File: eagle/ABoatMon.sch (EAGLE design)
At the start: 28 parts, among them J1 VUSB, J2 GND, J3 GND, X1 MKDSN1,5/2-5,08

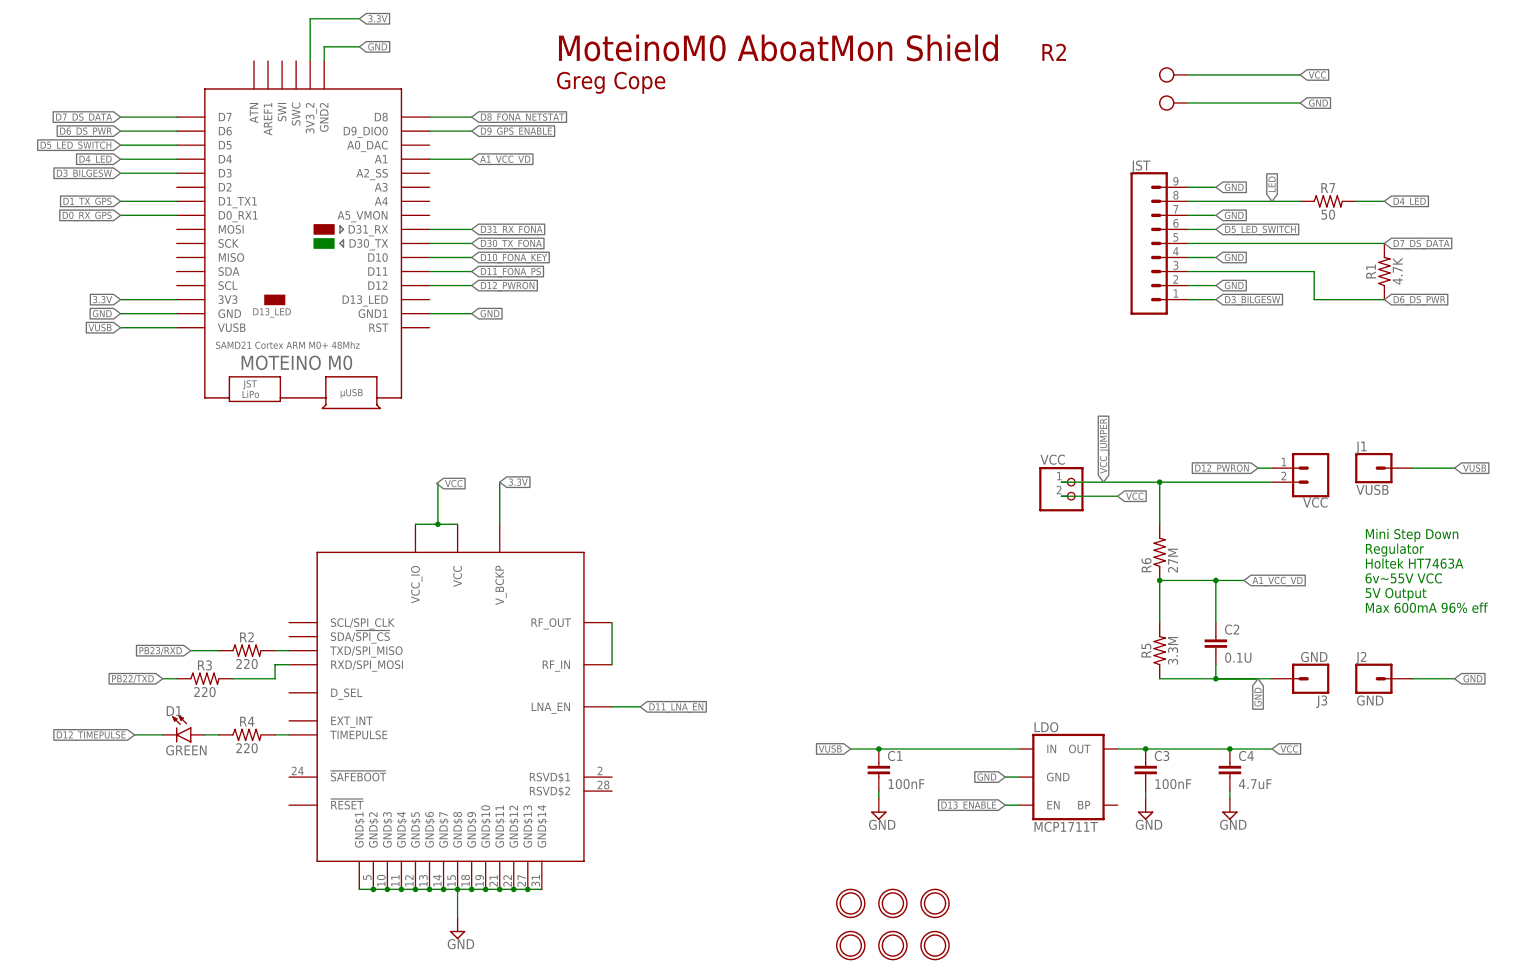
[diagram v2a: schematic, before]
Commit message: started adding nets
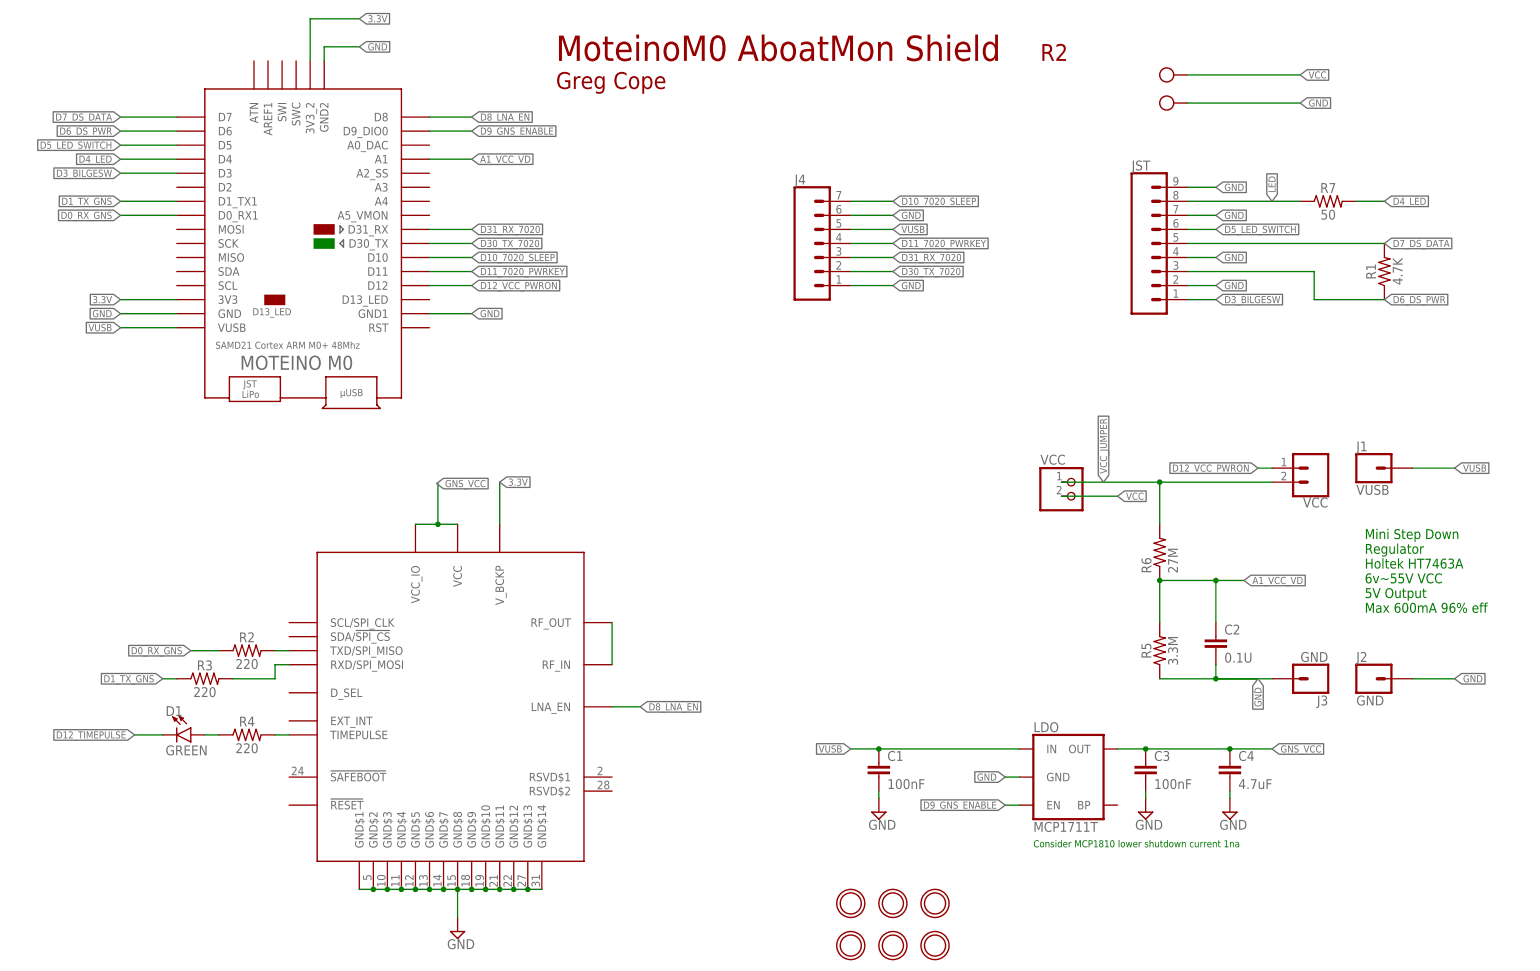
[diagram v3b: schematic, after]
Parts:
- added J4: (no value), SparkFun-Connectors:CONN_07
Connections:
- net D12_PWRON renamed D12_VCC_PWRON
- removed net D0_RX_GPS: U$6.D0_RX1
- removed net D10_FONA_KEY: U$6.D10
- removed net D11_FONA_PS: U$6.D11
- removed net D11_LNA_EN: U$5.LNA_EN
- removed net D13_ENABLE: LDO.EN
- removed net D1_TX_GPS: U$6.D1_TX1
- removed net D30_TX_FONA: U$6.D30_TX
- removed net D31_RX_FONA: U$6.D31_RX
- removed net D8_FONA_NETSTAT: U$6.D8
- removed net D9_GPS_ENABLE: U$6.D9_DIO0
- removed net PB22/TXD: R3.1
- removed net PB23/RXD: R2.1
- new net D0_RX_GNS: R2.1, U$6.D0_RX1
- new net D10_7020_SLEEP: J4.7, U$6.D10
- new net D11_7020_PWRKEY: J4.4, U$6.D11
- new net D1_TX_GNS: R3.1, U$6.D1_TX1
- new net D30_TX_7020: J4.2, U$6.D30_TX
- new net D31_RX_7020: J4.3, U$6.D31_RX
- new net D8_LNA_EN: U$5.LNA_EN, U$6.D8
- new net D9_GNS_ENABLE: LDO.EN, U$6.D9_DIO0
- new net GNS_VCC: C3.1, C4.1, LDO.OUT, U$5.VCC, U$5.VCC_IO
- net GND: now also J4.1, J4.6
- net VCC: no longer C3.1, C4.1, LDO.OUT, U$5.VCC, U$5.VCC_IO
- net VUSB: now also J4.5
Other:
- note added: "Consider MCP1810 lower shutdown current 1na"
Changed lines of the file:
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@@
 <part name="SUPPLY5" library="supply2" library_urn="urn:adsk.eagle:library:372" deviceset="GND" device=""/>
 <part name="D1" library="SparkFun-LED" library_urn="urn:adsk.eagle:library:529" deviceset="LED-GREEN" device="0603" package3d_urn="urn:adsk.eagle:package:39354/1" value="GREEN"/>
+<part name="J4" library="SparkFun-Connectors" library_urn="urn:adsk.eagle:library:513" deviceset="CONN_07" device="" package3d_urn="urn:adsk.eagle:package:38129/1"/>
 </parts>
 <sheets>
@@
 <text x="189.23" y="167.64" size="3.048" layer="94" ratio="12">R2</text>
 <text x="101.6" y="167.64" size="4.572" layer="94" ratio="15">MoteinoM0 AboatMon Shield</text>
+<text x="187.96" y="25.4" size="1.27" layer="91">Consider MCP1810 lower shutdown current 1na</text>
 </plain>
 <instances>
@@
 <attribute name="NAME" x="30.988" y="49.149" size="1.778" layer="95" font="vector"/>
 <attribute name="VALUE" x="30.988" y="43.815" size="1.778" layer="96" font="vector" align="top-left"/>
+</instance>
+<instance part="J4" gate="G$1" x="149.86" y="132.08" smashed="yes">
+<attribute name="VALUE" x="144.78" y="122.174" size="1.778" layer="96" font="vector"/>
+<attribute name="NAME" x="144.78" y="145.288" size="1.778" layer="95" font="vector"/>
 </instance>
 </instances>
@@
 <wire x1="223.52" y1="35.56" x2="223.52" y2="34.29" width="0.1524" layer="91"/>
 </segment>
+<segment>
+<pinref part="J4" gate="G$1" pin="1"/>
+<wire x1="154.94" y1="127" x2="162.56" y2="127" width="0.1524" layer="91"/>
+<label x="162.56" y="127" size="1.27" layer="95" xref="yes"/>
+</segment>
+<segment>
+<pinref part="J4" gate="G$1" pin="6"/>
+<wire x1="154.94" y1="139.7" x2="162.56" y2="139.7" width="0.1524" layer="91"/>
+<label x="162.56" y="139.7" size="1.27" layer="95" xref="yes"/>
+</segment>
 </net>
 <net name="VUSB" class="1">
@@
 <label x="154.94" y="43.18" size="1.27" layer="95" rot="R180" xref="yes"/>
 </segment>
+<segment>
+<pinref part="J4" gate="G$1" pin="5"/>
+<wire x1="154.94" y1="137.16" x2="162.56" y2="137.16" width="0.1524" layer="91"/>
+<label x="162.56" y="137.16" size="1.27" layer="95" xref="yes"/>
+</segment>
 </net>
 <net name="3.3V" class="1">
@@
 </segment>
 </net>
-<net name="D30_TX_FONA" class="0">
+<net name="D30_TX_7020" class="0">
 <segment>
 <wire x1="78.74" y1="134.62" x2="86.36" y2="134.62" width="0.1524" layer="91"/>
@@
 <label x="86.36" y="134.62" size="1.27" layer="95" xref="yes"/>
 </segment>
-</net>
-<net name="D8_FONA_NETSTAT" class="0">
-<segment>
-<pinref part="U$6" gate="G$1" pin="D8"/>
-<wire x1="78.74" y1="157.48" x2="86.36" y2="157.48" width="0.1524" layer="91"/>
-<label x="86.36" y="157.48" size="1.27" layer="95" xref="yes"/>
+<segment>
+<pinref part="J4" gate="G$1" pin="2"/>
+<wire x1="154.94" y1="129.54" x2="162.56" y2="129.54" width="0.1524" layer="91"/>
+<label x="162.56" y="129.54" size="1.27" layer="95" xref="yes"/>
 </segment>
 </net>
@@
 <pinref part="X1" gate="-1" pin="KL"/>
 <label x="236.22" y="165.1" size="1.27" layer="95" xref="yes"/>
-</segment>
-<segment>
-<pinref part="U$5" gate="G$1" pin="VCC_IO"/>
-<pinref part="U$5" gate="G$1" pin="VCC"/>
-<wire x1="76.2" y1="83.82" x2="80.264" y2="83.82" width="0.1524" layer="91"/>
-<label x="80.01" y="91.186" size="1.27" layer="95" xref="yes"/>
-<wire x1="80.264" y1="83.82" x2="83.82" y2="83.82" width="0.1524" layer="91"/>
-<wire x1="80.264" y1="91.186" x2="80.264" y2="83.82" width="0.1524" layer="91"/>
-<junction x="80.264" y="83.82"/>
-</segment>
-<segment>
-<pinref part="C3" gate="G$1" pin="1"/>
-<pinref part="LDO" gate="G$1" pin="OUT"/>
-<wire x1="203.2" y1="43.18" x2="208.28" y2="43.18" width="0.1524" layer="91"/>
-<junction x="208.28" y="43.18"/>
-<wire x1="208.28" y1="43.18" x2="223.52" y2="43.18" width="0.1524" layer="91"/>
-<label x="231.14" y="43.18" size="1.27" layer="95" xref="yes"/>
-<pinref part="C4" gate="G$1" pin="1"/>
-<wire x1="223.52" y1="43.18" x2="231.14" y2="43.18" width="0.1524" layer="91"/>
-<junction x="223.52" y="43.18"/>
 </segment>
 </net>
@@
 </segment>
 </net>
-<net name="D9_GPS_ENABLE" class="0">
+<net name="D9_GNS_ENABLE" class="0">
 <segment>
 <pinref part="U$6" gate="G$1" pin="D9_DIO0"/>
 <wire x1="78.74" y1="154.94" x2="86.36" y2="154.94" width="0.1524" layer="91"/>
 <label x="86.36" y="154.94" size="1.27" layer="95" xref="yes"/>
+</segment>
+<segment>
+<pinref part="LDO" gate="G$1" pin="EN"/>
+<wire x1="185.42" y1="33.02" x2="182.88" y2="33.02" width="0.1524" layer="91"/>
+<label x="182.88" y="33.02" size="1.27" layer="95" rot="R180" xref="yes"/>
 </segment>
 </net>
@@
 </segment>
 </net>
-<net name="D1_TX_GPS" class="0">
+<net name="D1_TX_GNS" class="0">
 <segment>
 <pinref part="U$6" gate="G$1" pin="D1_TX1"/>
@@
 <label x="22.86" y="142.24" size="1.27" layer="95" rot="R180" xref="yes"/>
 </segment>
-</net>
-<net name="D0_RX_GPS" class="0">
+<segment>
+<pinref part="R3" gate="G$1" pin="1"/>
+<wire x1="33.02" y1="55.88" x2="30.48" y2="55.88" width="0.1524" layer="91"/>
+<label x="30.48" y="55.88" size="1.27" layer="95" rot="R180" xref="yes"/>
+</segment>
+</net>
+<net name="D0_RX_GNS" class="0">
 <segment>
 <pinref part="U$6" gate="G$1" pin="D0_RX1"/>
@@
 <label x="22.86" y="139.7" size="1.27" layer="95" rot="R180" xref="yes"/>
 </segment>
-</net>
-<net name="D31_RX_FONA" class="0">
+<segment>
+<pinref part="R2" gate="G$1" pin="1"/>
+<wire x1="40.64" y1="60.96" x2="35.56" y2="60.96" width="0.1524" layer="91"/>
+<label x="35.56" y="60.96" size="1.27" layer="95" rot="R180" xref="yes"/>
+</segment>
+</net>
+<net name="D31_RX_7020" class="0">
 <segment>
 <pinref part="U$6" gate="G$1" pin="D31_RX"/>
 <wire x1="78.74" y1="137.16" x2="86.36" y2="137.16" width="0.1524" layer="91"/>
 <label x="86.36" y="137.16" size="1.27" layer="95" xref="yes"/>
+</segment>
+<segment>
+<pinref part="J4" gate="G$1" pin="3"/>
+<wire x1="154.94" y1="132.08" x2="162.56" y2="132.08" width="0.1524" layer="91"/>
+<label x="162.56" y="132.08" size="1.27" layer="95" xref="yes"/>
 </segment>
 </net>
@@
 </segment>
 </net>
-<net name="D12_PWRON" class="0">
+<net name="D12_VCC_PWRON" class="0">
 <segment>
 <pinref part="U$6" gate="G$1" pin="D12"/>
@@
 </segment>
 </net>
-<net name="D10_FONA_KEY" class="0">
+<net name="D10_7020_SLEEP" class="0">
 <segment>
 <pinref part="U$6" gate="G$1" pin="D10"/>
@@
 <label x="86.36" y="132.08" size="1.27" layer="95" xref="yes"/>
 </segment>
-</net>
-<net name="D11_FONA_PS" class="0">
+<segment>
+<pinref part="J4" gate="G$1" pin="7"/>
+<wire x1="154.94" y1="142.24" x2="162.56" y2="142.24" width="0.1524" layer="91"/>
+<label x="162.56" y="142.24" size="1.27" layer="95" xref="yes"/>
+</segment>
+</net>
+<net name="D11_7020_PWRKEY" class="0">
 <segment>
 <pinref part="U$6" gate="G$1" pin="D11"/>
@@
 <label x="86.36" y="129.54" size="1.27" layer="95" xref="yes"/>
 </segment>
-</net>
-<net name="PB22/TXD" class="0">
-<segment>
-<pinref part="R3" gate="G$1" pin="1"/>
-<wire x1="33.02" y1="55.88" x2="30.48" y2="55.88" width="0.1524" layer="91"/>
-<label x="30.48" y="55.88" size="1.27" layer="95" rot="R180" xref="yes"/>
-</segment>
-</net>
-<net name="PB23/RXD" class="0">
-<segment>
-<pinref part="R2" gate="G$1" pin="1"/>
-<wire x1="40.64" y1="60.96" x2="35.56" y2="60.96" width="0.1524" layer="91"/>
-<label x="35.56" y="60.96" size="1.27" layer="95" rot="R180" xref="yes"/>
+<segment>
+<pinref part="J4" gate="G$1" pin="4"/>
+<wire x1="154.94" y1="134.62" x2="162.56" y2="134.62" width="0.1524" layer="91"/>
+<label x="162.56" y="134.62" size="1.27" layer="95" xref="yes"/>
 </segment>
 </net>
@@
 </segment>
 </net>
-<net name="D11_LNA_EN" class="0">
+<net name="D8_LNA_EN" class="0">
 <segment>
 <pinref part="U$5" gate="G$1" pin="LNA_EN"/>
@@
 <label x="116.84" y="50.8" size="1.27" layer="95" xref="yes"/>
 </segment>
-</net>
-<net name="D13_ENABLE" class="0">
-<segment>
-<pinref part="LDO" gate="G$1" pin="EN"/>
-<wire x1="185.42" y1="33.02" x2="182.88" y2="33.02" width="0.1524" layer="91"/>
-<label x="182.88" y="33.02" size="1.27" layer="95" rot="R180" xref="yes"/>
+<segment>
+<pinref part="U$6" gate="G$1" pin="D8"/>
+<wire x1="78.74" y1="157.48" x2="86.36" y2="157.48" width="0.1524" layer="91"/>
+<label x="86.36" y="157.48" size="1.27" layer="95" xref="yes"/>
 </segment>
 </net>
@@
 </segment>
 </net>
+<net name="GNS_VCC" class="1">
+<segment>
+<pinref part="C3" gate="G$1" pin="1"/>
+<pinref part="LDO" gate="G$1" pin="OUT"/>
+<wire x1="203.2" y1="43.18" x2="208.28" y2="43.18" width="0.1524" layer="91"/>
+<junction x="208.28" y="43.18"/>
+<wire x1="208.28" y1="43.18" x2="223.52" y2="43.18" width="0.1524" layer="91"/>
+<label x="231.14" y="43.18" size="1.27" layer="95" xref="yes"/>
+<pinref part="C4" gate="G$1" pin="1"/>
+<wire x1="223.52" y1="43.18" x2="231.14" y2="43.18" width="0.1524" layer="91"/>
+<junction x="223.52" y="43.18"/>
+</segment>
+<segment>
+<pinref part="U$5" gate="G$1" pin="VCC_IO"/>
+<pinref part="U$5" gate="G$1" pin="VCC"/>
+<wire x1="76.2" y1="83.82" x2="80.264" y2="83.82" width="0.1524" layer="91"/>
+<label x="80.01" y="91.186" size="1.27" layer="95" xref="yes"/>
+<wire x1="80.264" y1="83.82" x2="83.82" y2="83.82" width="0.1524" layer="91"/>
+<wire x1="80.264" y1="91.186" x2="80.264" y2="83.82" width="0.1524" layer="91"/>
+<junction x="80.264" y="83.82"/>
+</segment>
+</net>
